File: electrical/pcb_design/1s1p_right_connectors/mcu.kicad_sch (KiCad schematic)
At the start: 14 parts, among them J17 STLINK_TagConnect_6, U1 BMI323, U2 BMI323, U4 STM32L452CEU6

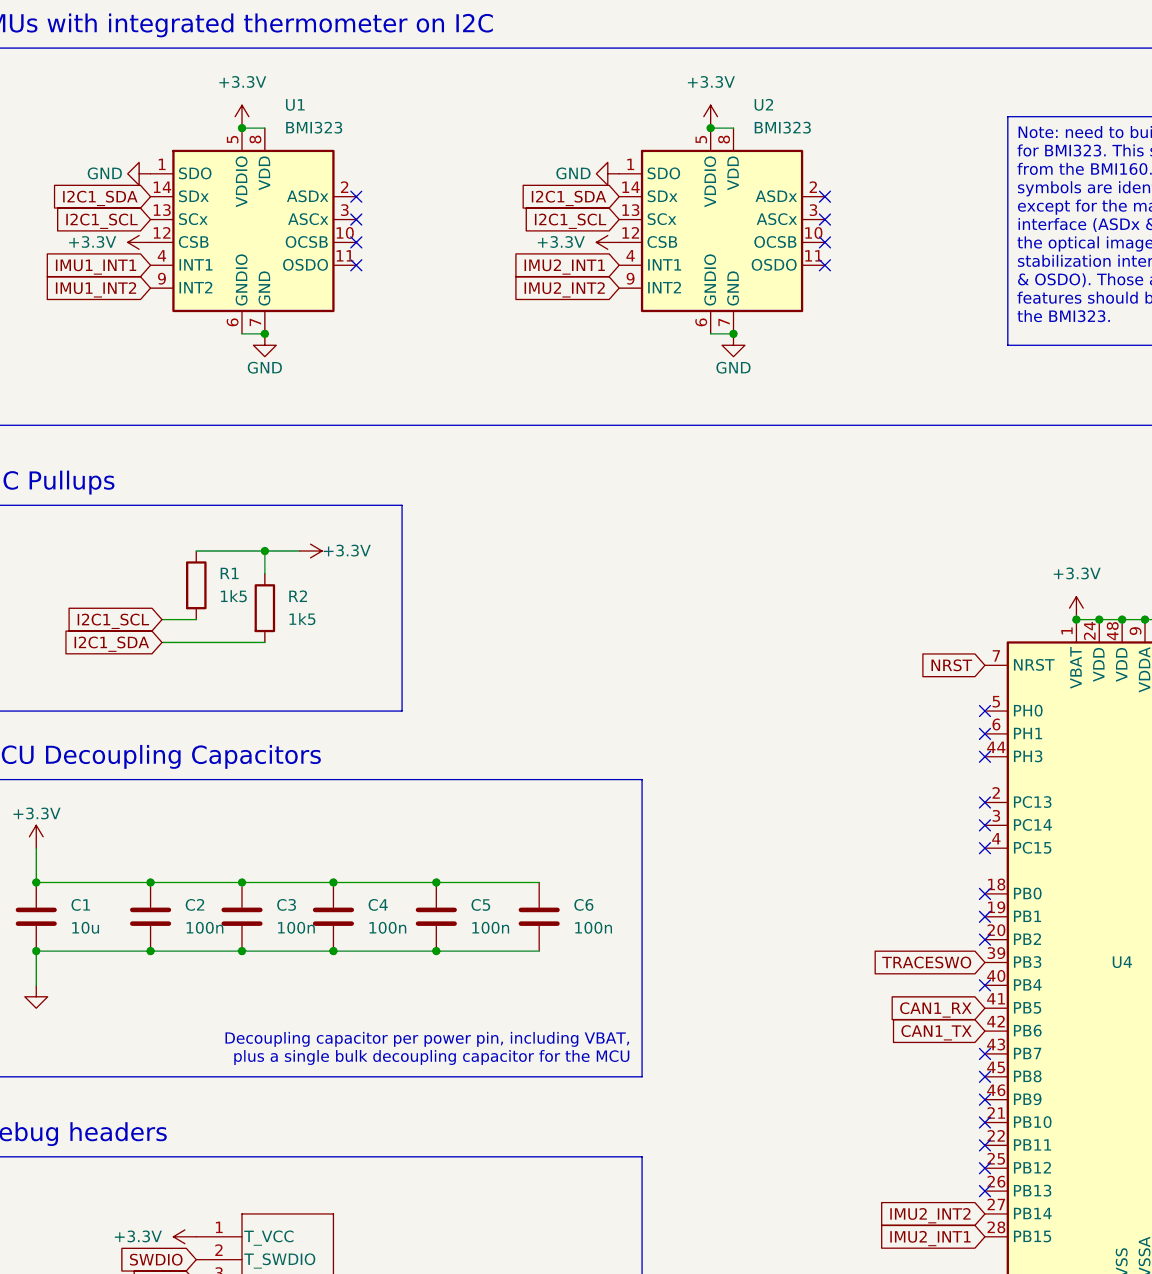
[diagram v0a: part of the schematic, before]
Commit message: Regenerated 1s1p battery boards from 2s1p battery board
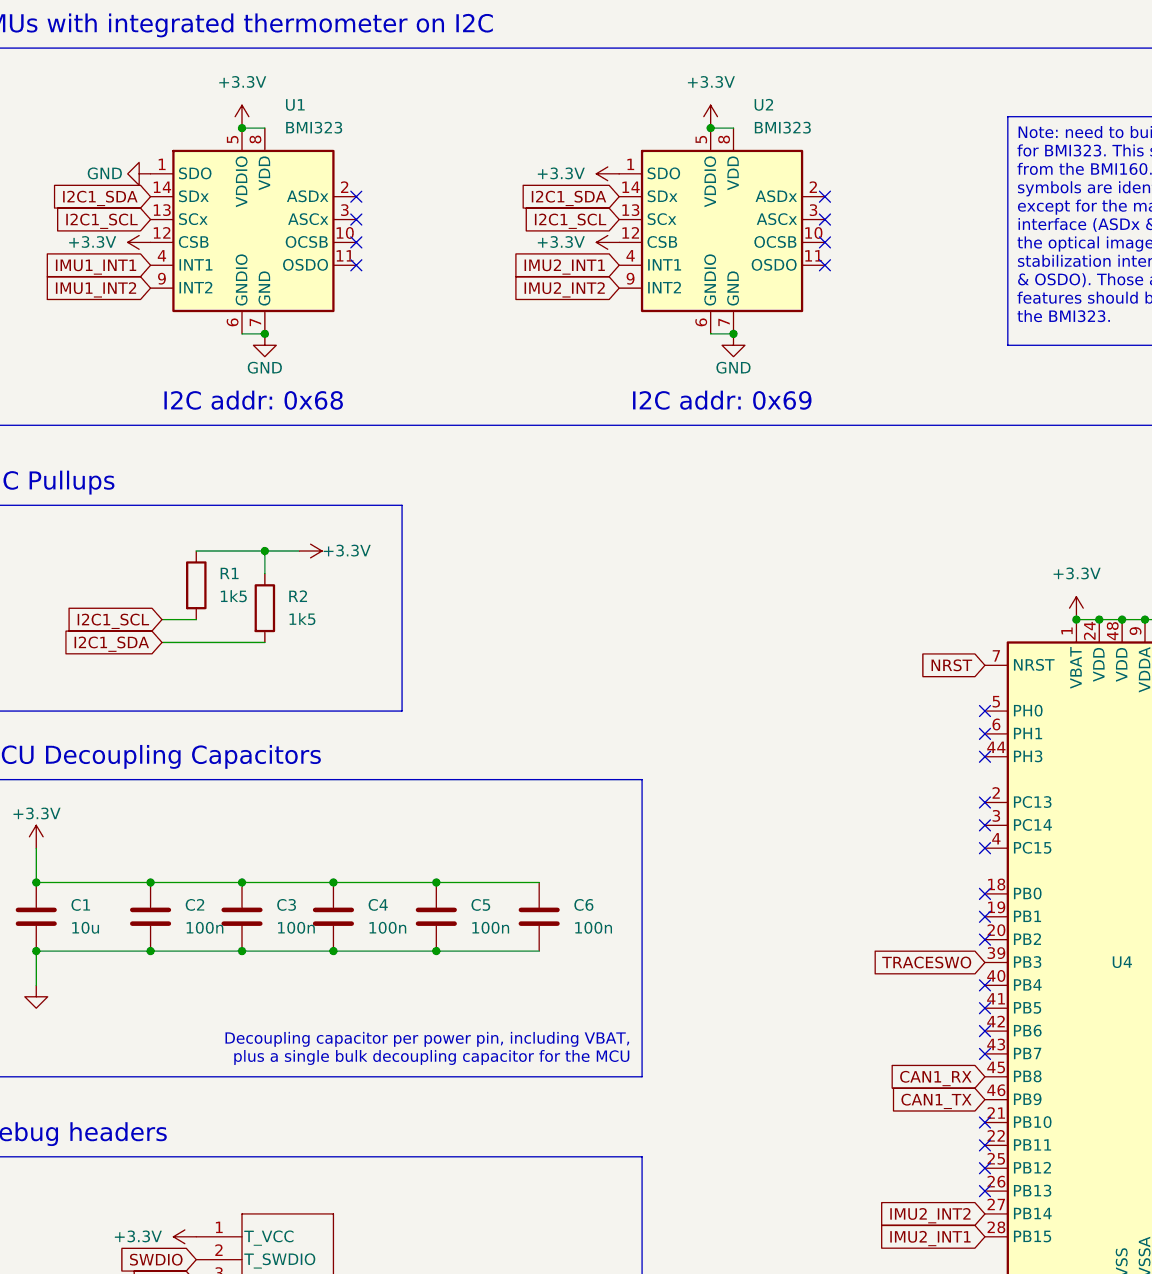
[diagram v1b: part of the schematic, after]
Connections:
- net +3.3V: now also U2.1 (SDO)
- net CAN1_RX: now also U4.45 (PB8); no longer U4.41 (PB5)
- net CAN1_TX: now also U4.46 (PB9); no longer U4.42 (PB6)
- net GND: no longer U2.1 (SDO)
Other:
- note added: "I2C addr: 0x68"
- note added: "I2C addr: 0x69"

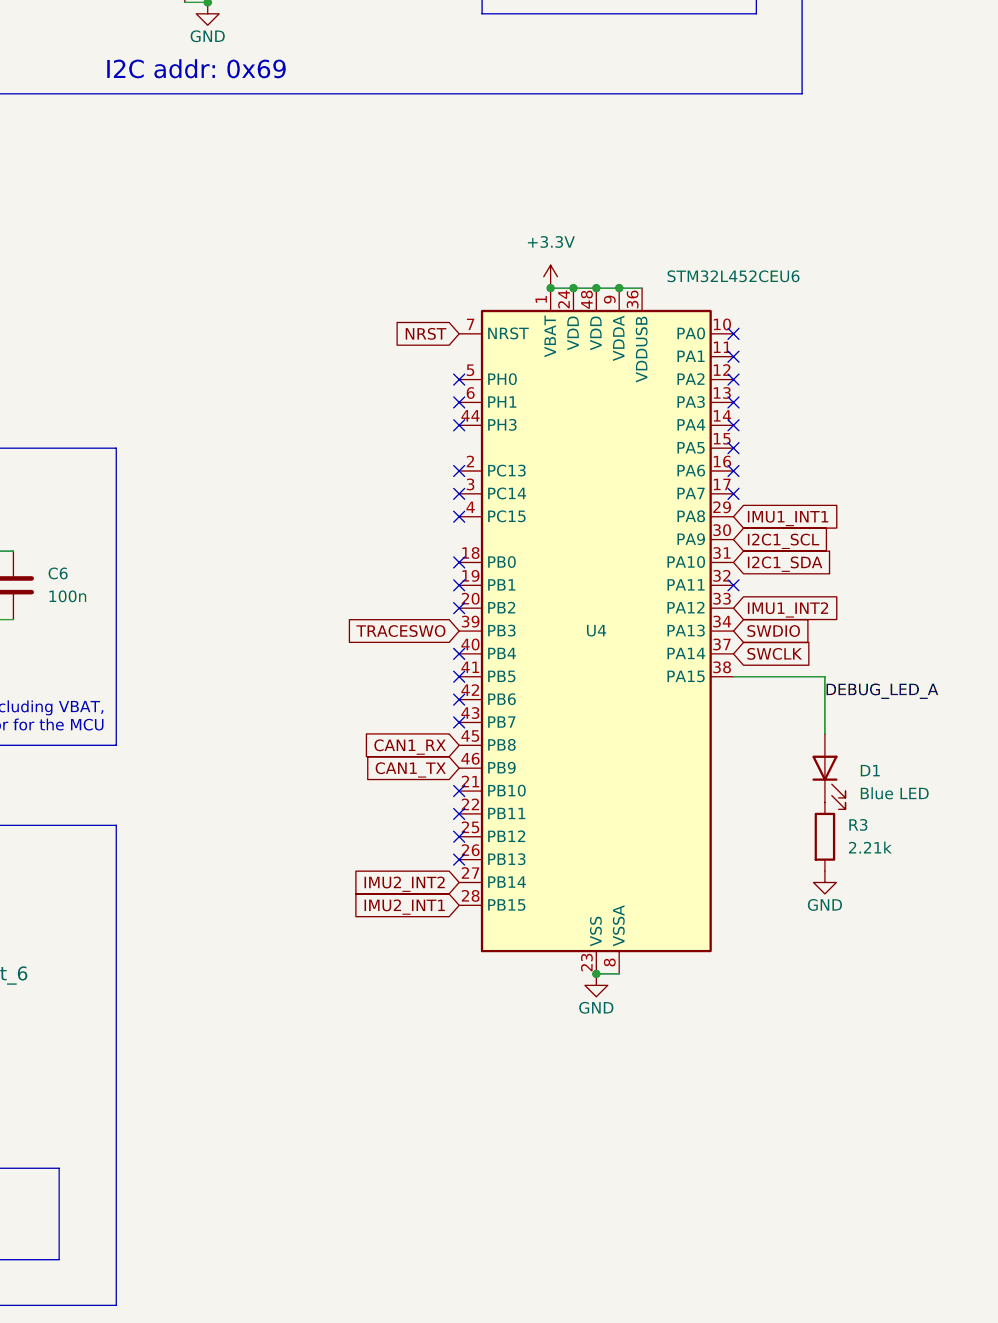
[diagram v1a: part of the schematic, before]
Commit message: Added board identification mechanism. Updated production files and 3D models.
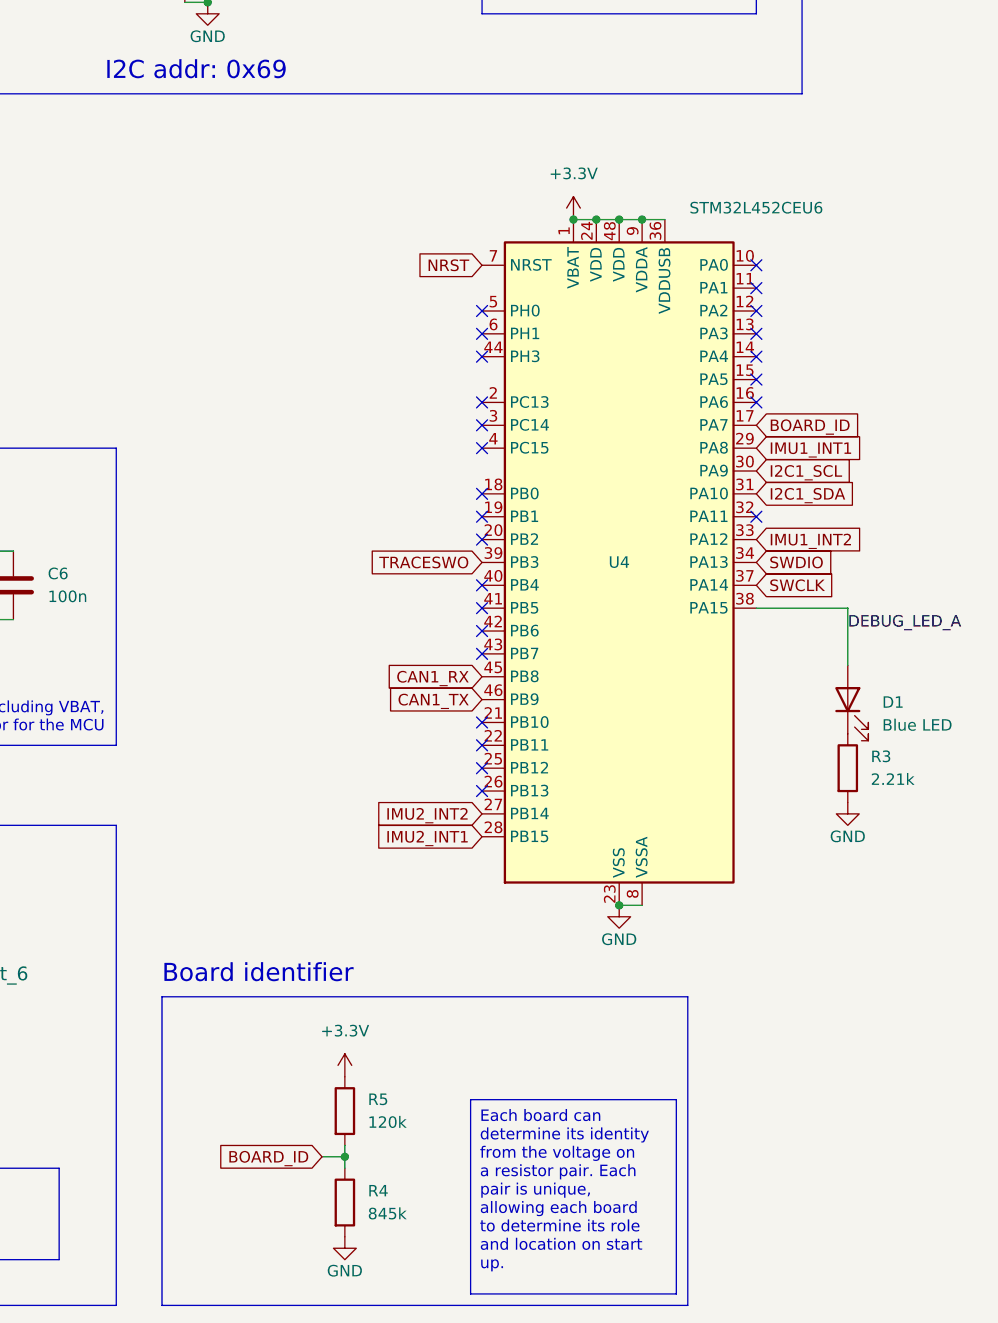
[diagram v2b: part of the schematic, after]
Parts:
- added R4: 845k, footprints:Nondescript_R_0402_1005Metric, symbol Device:R
- added R5: 120k, footprints:Nondescript_R_0402_1005Metric, symbol Device:R
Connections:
- net +3.3V: now also R5.1
- net GND: now also R4.2
- net BOARD_ID: now reaches U4.17 (PA7)
- net BOARD_ID: now also R4.1, R5.2
- no-connect marks 34 -> 33
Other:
- note added: "Board identifier"
- moved on the sheet: D1, R3, U4

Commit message: Modified PCB designs to use local footprint for the STM32L452CEU6 part in order to configure the 3D model for this part.
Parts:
- U4: footprint Package_DFN_QFN:QFN-48-1EP_7x7mm_P0.5mm_EP5.6x5.6mm -> footprints:QFN-48-1EP_7x7mm_P0.5mm_EP5.6x5.6mm_ThermalVias
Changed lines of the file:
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@@
       (effects (font (size 1.27 1.27)) (justify left) hide)
     )
-    (property "Footprint" "Package_DFN_QFN:QFN-48-1EP_7x7mm_P0.5mm_EP5.6x5.6mm" (at 134.62 148.59 0)
+    (property "Footprint" "footprints:QFN-48-1EP_7x7mm_P0.5mm_EP5.6x5.6mm_ThermalVias" (at 134.62 148.59 0)
       (effects (font (size 1.27 1.27)) (justify right) hide)
     )

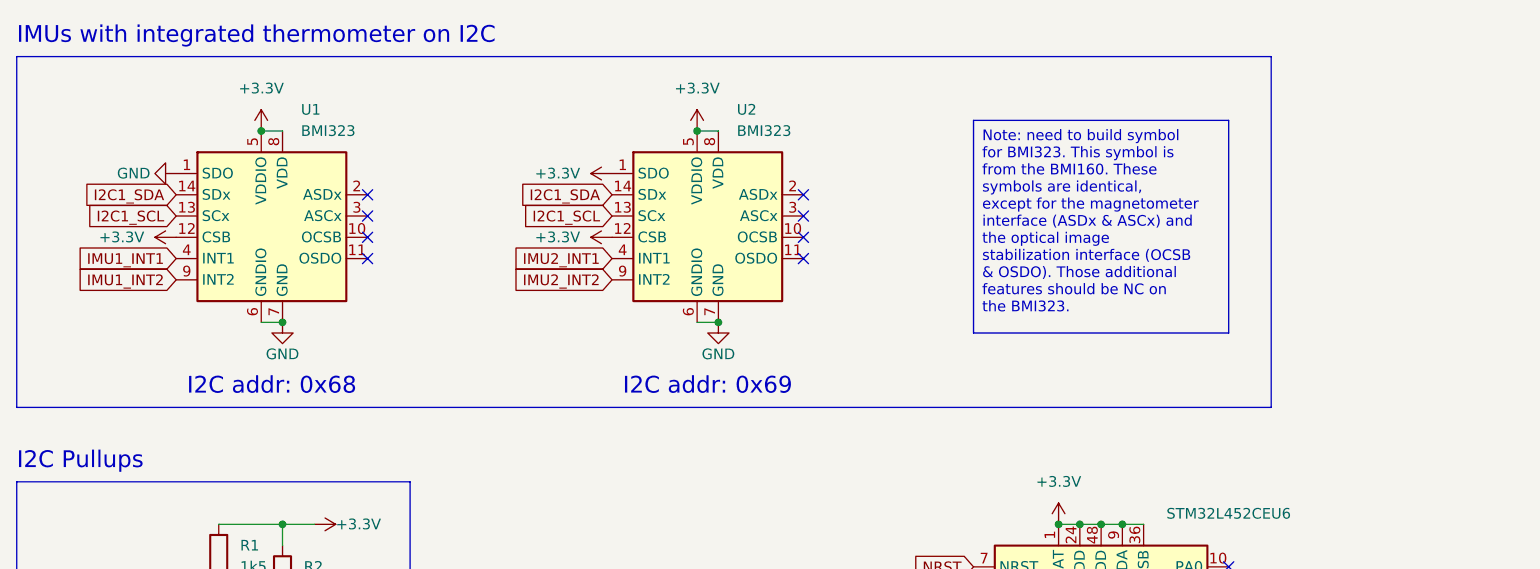
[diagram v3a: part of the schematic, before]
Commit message: Added decoupling capacitors for IMUs on battery boards
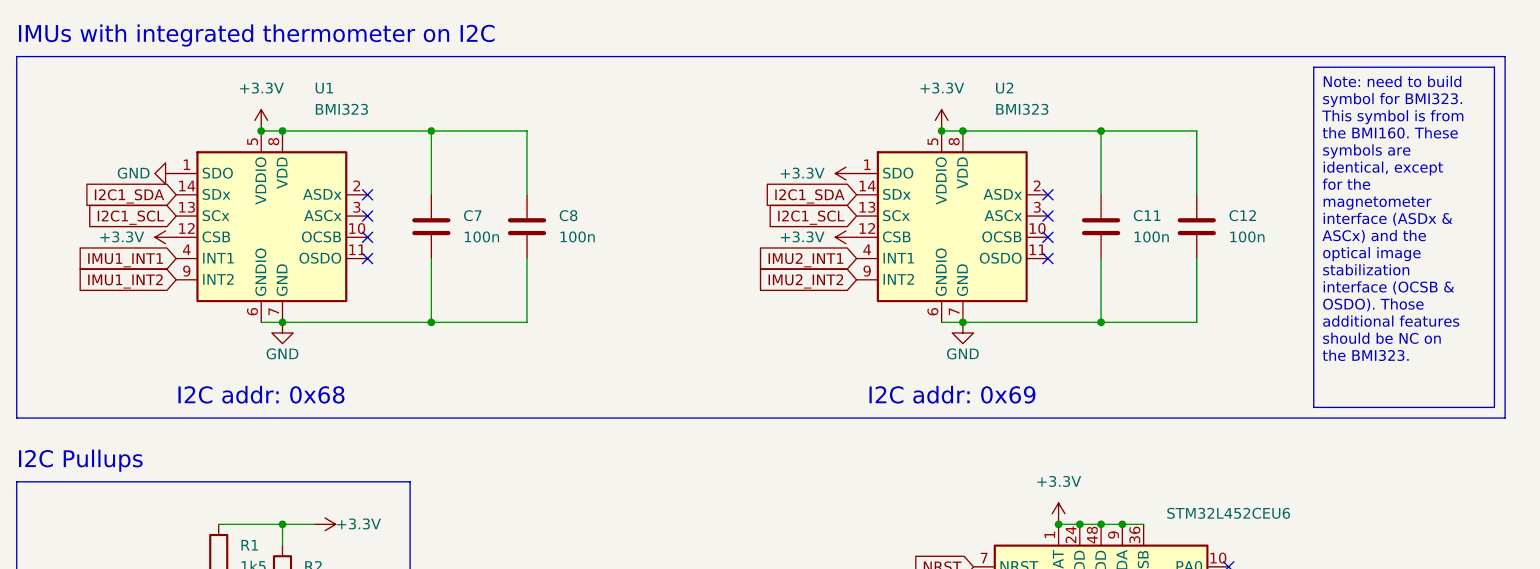
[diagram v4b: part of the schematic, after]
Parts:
- added C11, C12, C7, C8: 100n, footprints:Nondescript_C_0402_1005Metric, symbol TVSC:Small_Decoupling_Capacitor
- U1, U2: Tmax (none) -> 85; Tmin (none) -> -40; Tsensitivity (none) -> 2%
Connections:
- net +3.3V: now also C11.1, C12.1, C7.1, C8.1
- net GND: now also C11.2, C12.2, C7.2, C8.2
